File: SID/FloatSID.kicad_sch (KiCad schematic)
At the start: 18 parts, among them M1 Motor_DC, SW1 SW, SW2 Limit Switch, U2 MS583730BA01-50, U4 XiaoESP32C3

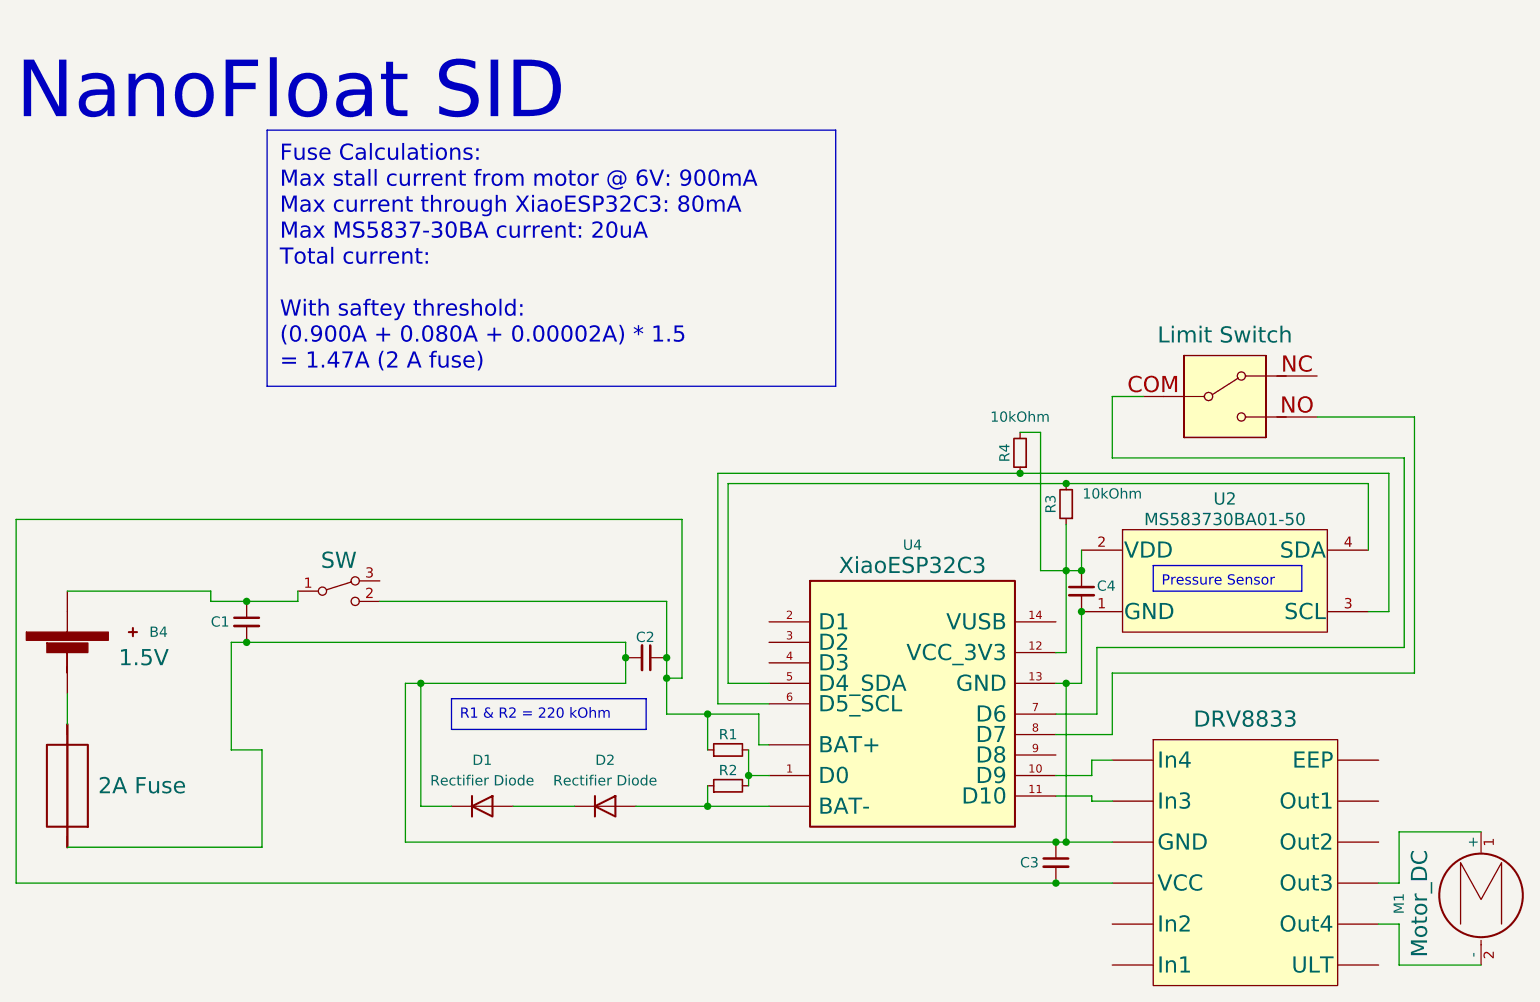
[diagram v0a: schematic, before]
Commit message: Full Rework of NanoBoard Libraries, Updated Final Version of NB101
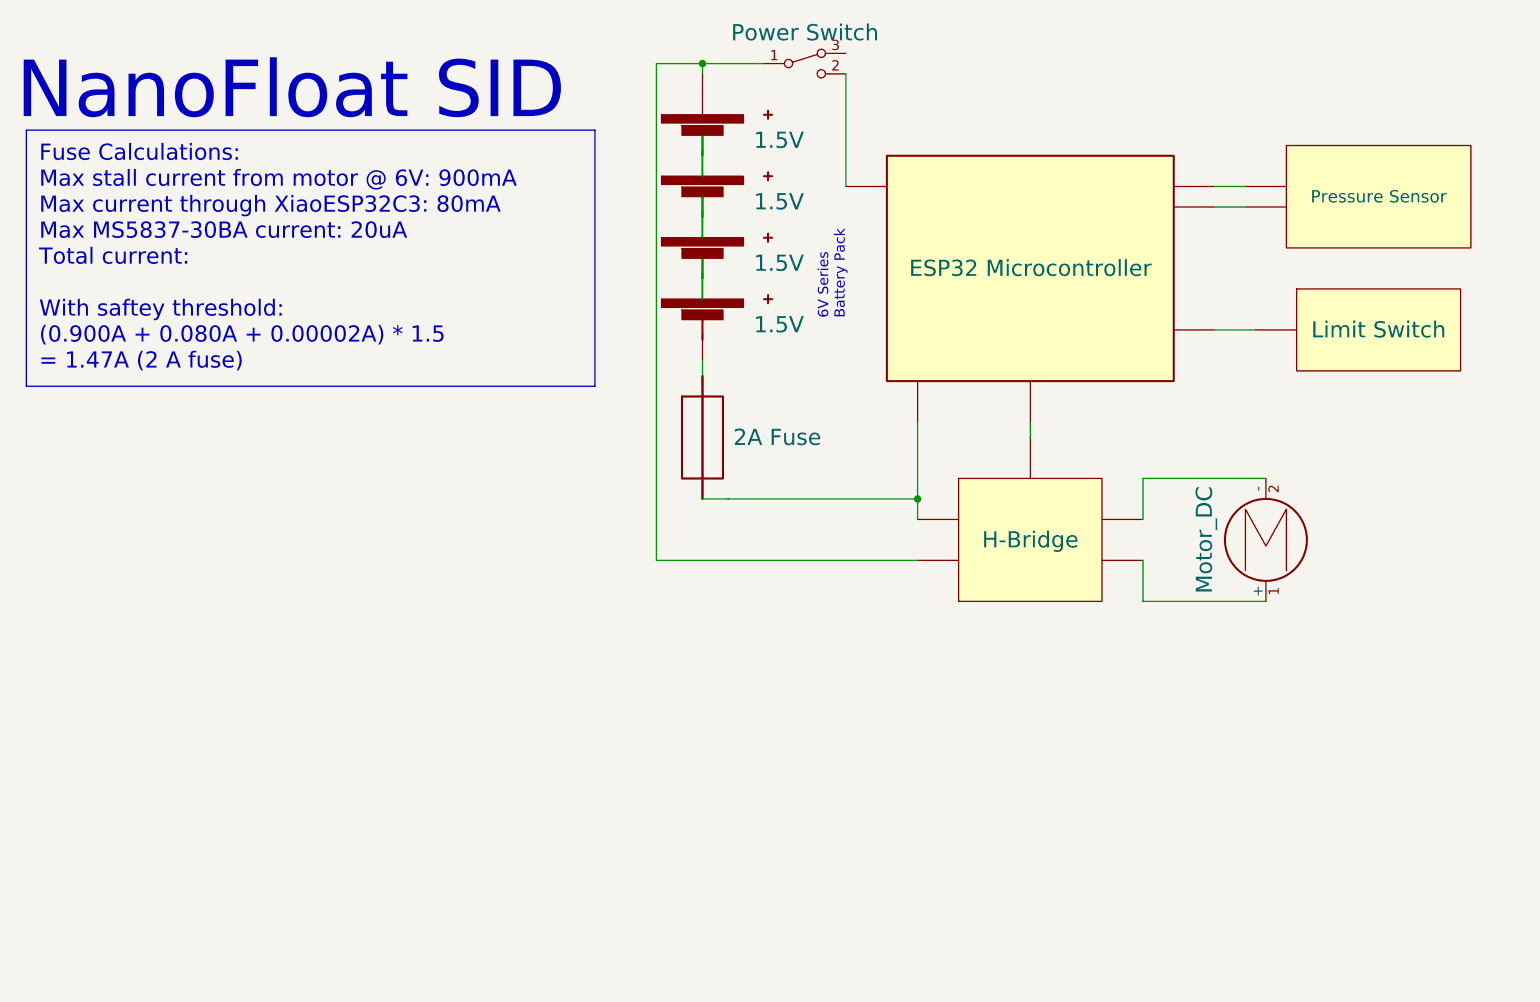
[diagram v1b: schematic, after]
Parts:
- removed C1, C2, C3, C4: C_Small, Capacitor_SMD:C_1812_4532Metric_Pad1.57x3.40mm_HandSolder, symbol Device:C_Small
- removed D1, D2: Rectifier Diode, Diode_THT:D_DO-41_SOD81_P10.16mm_Horizontal, symbol Diode:1N4001
- removed R1, R2: 220kOhm, Resistor_THT:R_Axial_DIN0207_L6.3mm_D2.5mm_P7.62mm_Horizontal, symbol Device:R_Small
- removed R3, R4: 10kOhm, Resistor_THT:R_Axial_DIN0207_L6.3mm_D2.5mm_P7.62mm_Horizontal, symbol Device:R_Small
- added B1, B2, B3: 1.5V, Connector_PinHeader_2.54mm:PinHeader_1x02_P2.54mm_Vertical, symbol Device:Battery_Cell
- H-Bridge: renamed from DRV8833; footprint DRV8833:DRV8833 -> NanoFloat Pressure Sensor:DRV8220DRLR
- SW1: value SW -> Power Switch
- U2: value MS583730BA01-50 -> Pressure Sensor
- U4: value XiaoESP32C3 -> ESP32 Microcontroller
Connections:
- net at SW1.2 (B), U4.: no longer H-Bridge. (VCC)
- net at F1.2: now also H-Bridge., U4.; no longer B4.2 (-)
- net at H-Bridge.: now also B4.1 (+), SW1.1 (A)
- new net: U2., U4. (x2)
- new net: SW2., U4.
- new net: B3.2 (-), F1.1
- new net: H-Bridge., U4.
- new net: B1.2 (-), B2.1 (+)
- new net: B2.2 (-), B3.1 (+)
- new net: B1.1 (+), B4.2 (-)
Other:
- note added: "6V Series Battery Pack"
